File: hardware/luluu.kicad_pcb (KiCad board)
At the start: 2 copper layers, 75 x 30 mm, 53 parts, among them J1 BATT_CON, J2 RPi SWD, J3 STEMMA_{QT} I_{2}C, J4 Micro_SD_Card, J5 RPi UART, J6 USB_C_Receptacle_USB2.0, J7 DISP_LCD_ST7789, Q1 AO3401A, Q2 BSS138, SW1 SW_USBBOOT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

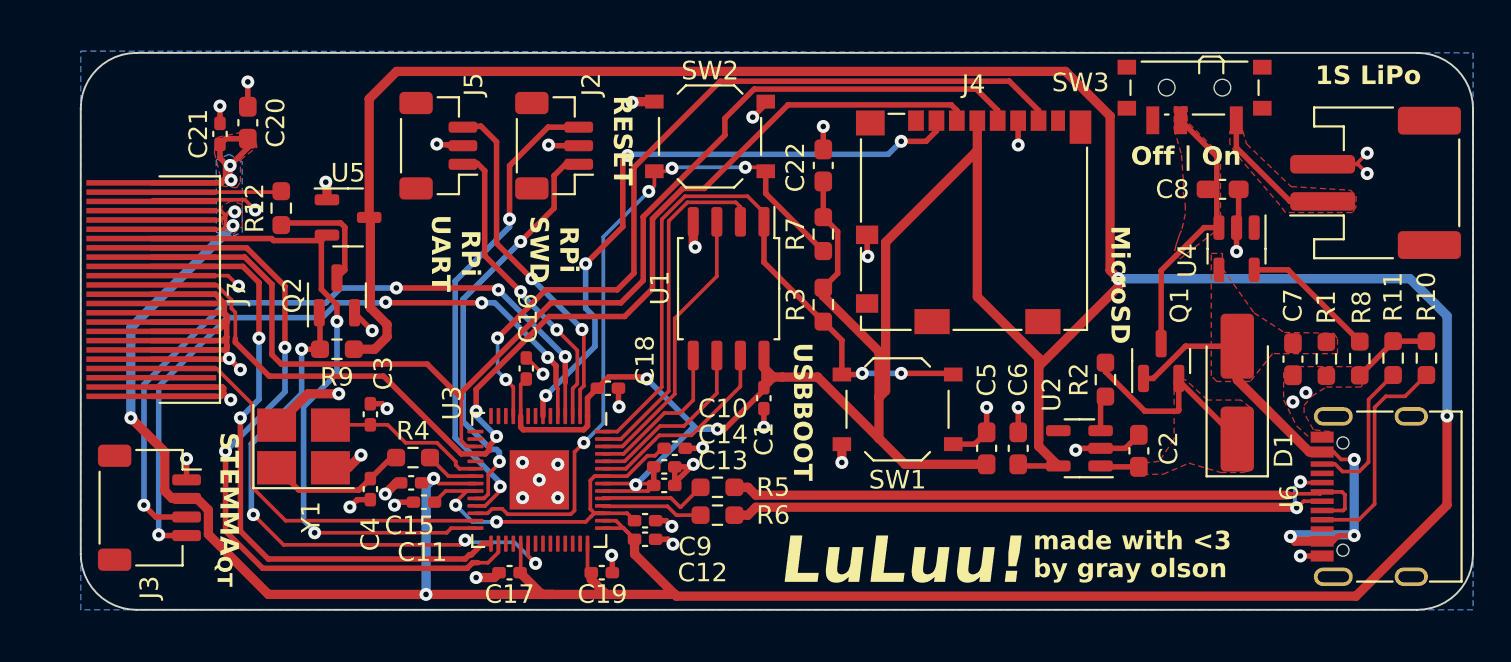
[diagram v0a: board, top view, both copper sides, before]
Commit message: layout improvements and jlcpcb part positioning offsets
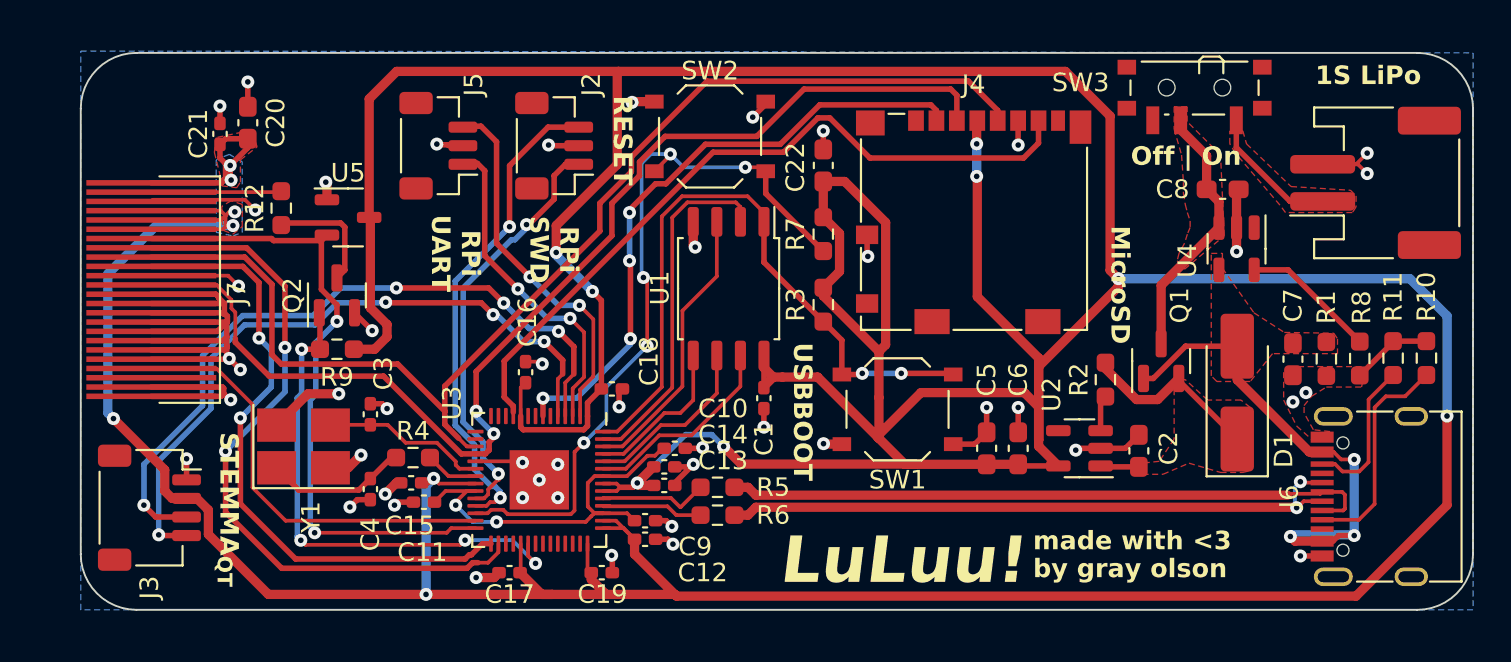
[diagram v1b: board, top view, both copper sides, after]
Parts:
- moved C18 0.22 mm to (140.8, 96.3)
- moved C16 0.20 mm to (136.2, 95.5)
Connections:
- U3 pad 19: unconnected-(U3-TESTEN-Pad19) -> GND
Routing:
- net +3V3: track 349.3 -> 380.0 mm, vias 12 -> 15
- net SPI_{MISO}: track 44.0 -> 39.6 mm, vias 2 -> 0
- net Net-(U3-RUN): track 37.5 -> 40.2 mm, vias 4 -> 5
- net DISP BACKLIGHT: track 30.7 -> 28.0 mm
- net GND: track 119.3 -> 121.6 mm
- net Net-(D1-K): track 13.7 -> 12.1 mm
- net UART_{TX}: track 19.0 -> 20.0 mm
- net UART_{RX}: track 16.7 -> 17.7 mm
- net SPI_{MOSI}: track 62.3 -> 63.2 mm
- net DISP ~{CS_{MAIN}}: track 38.9 -> 38.3 mm

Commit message: final_prod
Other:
- board text added: "+"
- board text added: "-"
- board text added: "v0"
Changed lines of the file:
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@@
     (effects (font (size 1 1) (thickness 0.2) bold) (justify left bottom))
   )
-  (gr_text "LuLuu!" (at 149.8375 107.05) (layer "F.SilkS")
+  (gr_text "+" (at 175.35 87.05) (layer "F.SilkS")
+    (effects (font (size 1.5 1.5) (thickness 0.3) bold) (justify left bottom))
+  )
+  (gr_text "LuLuu!" (at 148.45 107) (layer "F.SilkS")
     (effects (font (size 2.5 2.5) (thickness 0.4) bold italic) (justify left bottom))
   )
   (gr_text "RPi\nSWD" (at 136.3375 88.85 -90) (layer "F.SilkS")
     (effects (font (size 1 1) (thickness 0.2) bold) (justify bottom))
+  )
+  (gr_text "-" (at 177.2 85.35 90) (layer "F.SilkS")
+    (effects (font (size 1.5 1.5) (thickness 0.3) bold) (justify left bottom))
   )
   (gr_text "RESET" (at 140.8375 80.55 -90) (layer "F.SilkS")
@@
     (effects (font (size 1 1) (thickness 0.2) bold) (justify left bottom))
   )
+  (gr_text "v0" (at 160.65 106.85) (layer "F.SilkS")
+    (effects (font (size 1 1) (thickness 0.2) bold italic) (justify left bottom))
+  )
   (gr_text "RPi\nUART" (at 131.0375 89.05 -90) (layer "F.SilkS")

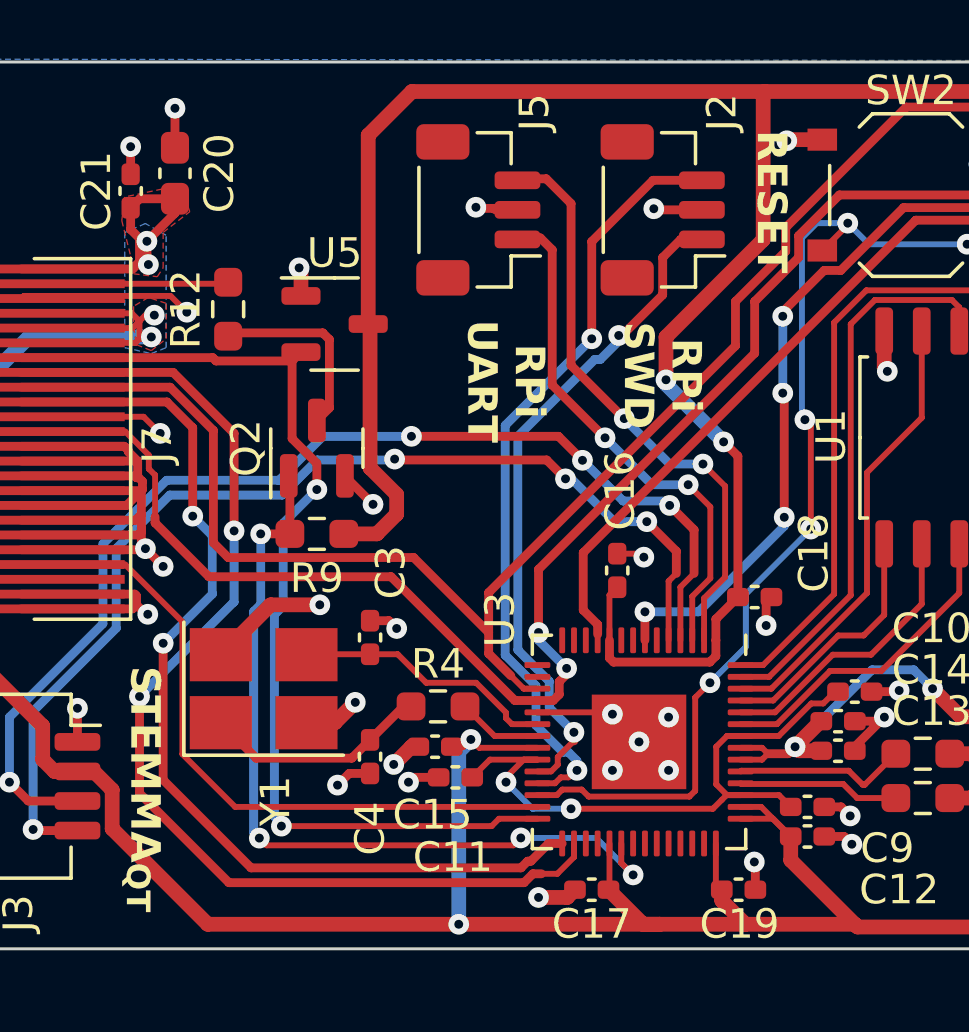
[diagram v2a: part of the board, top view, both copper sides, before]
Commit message: add pullups to disp reset, disp csmain, card cs
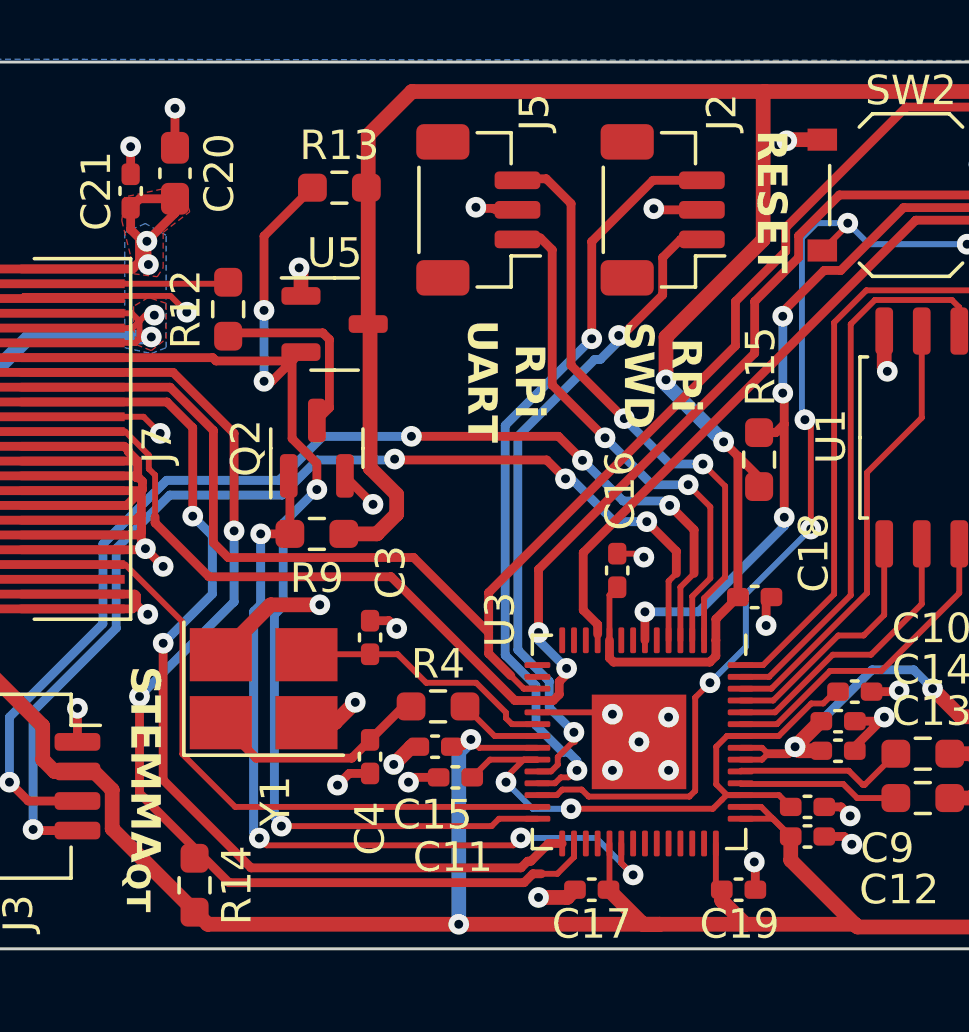
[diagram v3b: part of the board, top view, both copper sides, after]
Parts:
- added R13: 10k, Resistor_SMD:R_0603_1608Metric_Pad0.98x0.95mm_HandSolder, F.Cu at (126.8, 82.5)
- added R14: 10k, Resistor_SMD:R_0603_1608Metric_Pad0.98x0.95mm_HandSolder, F.Cu at (121.9, 106.1)
- added R15: 10k, Resistor_SMD:R_0603_1608Metric_Pad0.98x0.95mm_HandSolder, F.Cu at (141.0, 91.7)
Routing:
- net DISP ~{RESET}: track 35.1 -> 43.6 mm, vias 2 -> 4
- net +3V3: track 380.0 -> 381.3 mm
- net CARD ~{CS}: track 33.7 -> 34.7 mm

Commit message: rev1
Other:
- board text added: "v1"
- board text removed: "v0"
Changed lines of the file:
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@@
   (title_block
     (title "LuLuu!")
-    (date "2023-10-14")
-    (rev "0")
+    (date "2023-10-17")
+    (rev "1")
     (company "Gray Olson")
     (comment 1 "Made with love by")
@@
     (effects (font (size 1 1) (thickness 0.2) bold) (justify left bottom))
   )
-  (gr_text "v0" (at 160.65 106.85) (layer "F.SilkS")
+  (gr_text "v1" (at 160.65 106.85) (layer "F.SilkS")
     (effects (font (size 1 1) (thickness 0.2) bold italic) (justify left bottom))
   )

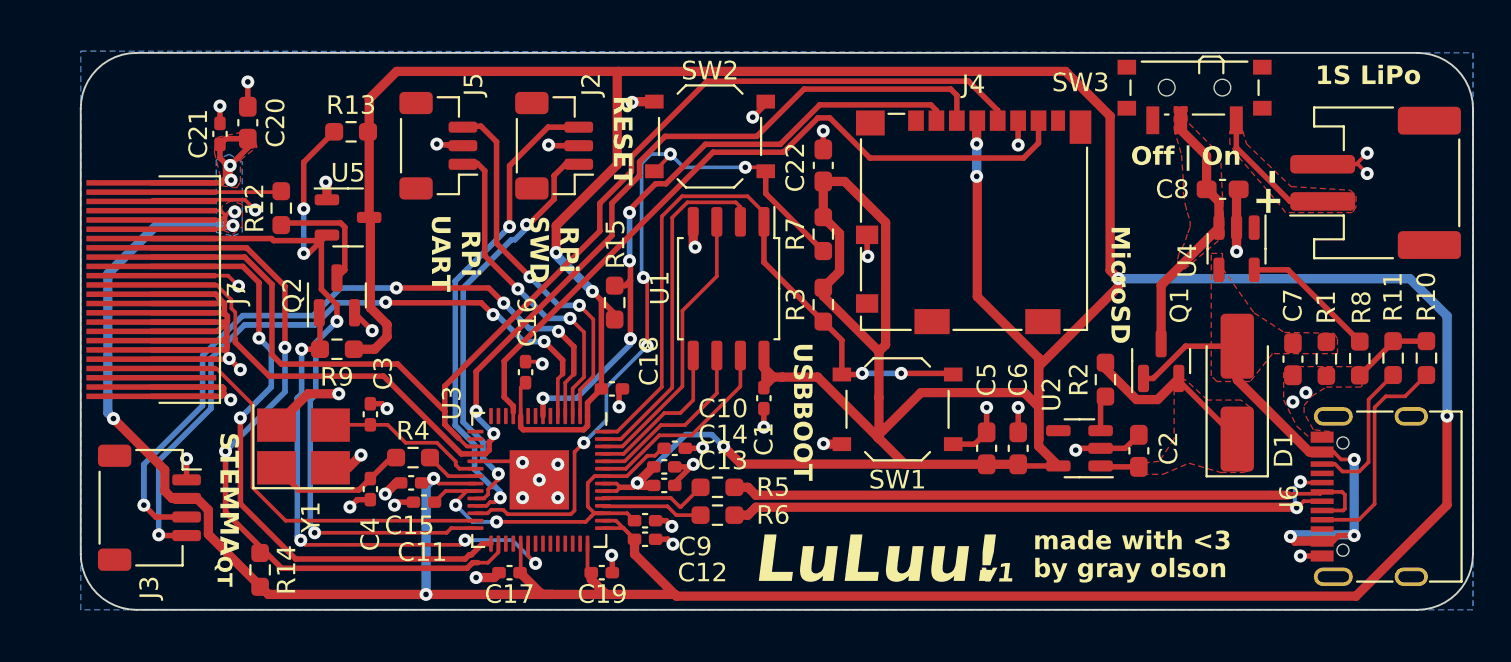
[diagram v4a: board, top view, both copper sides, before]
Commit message: rev1.1 - fix USB data and 1k boot resistor
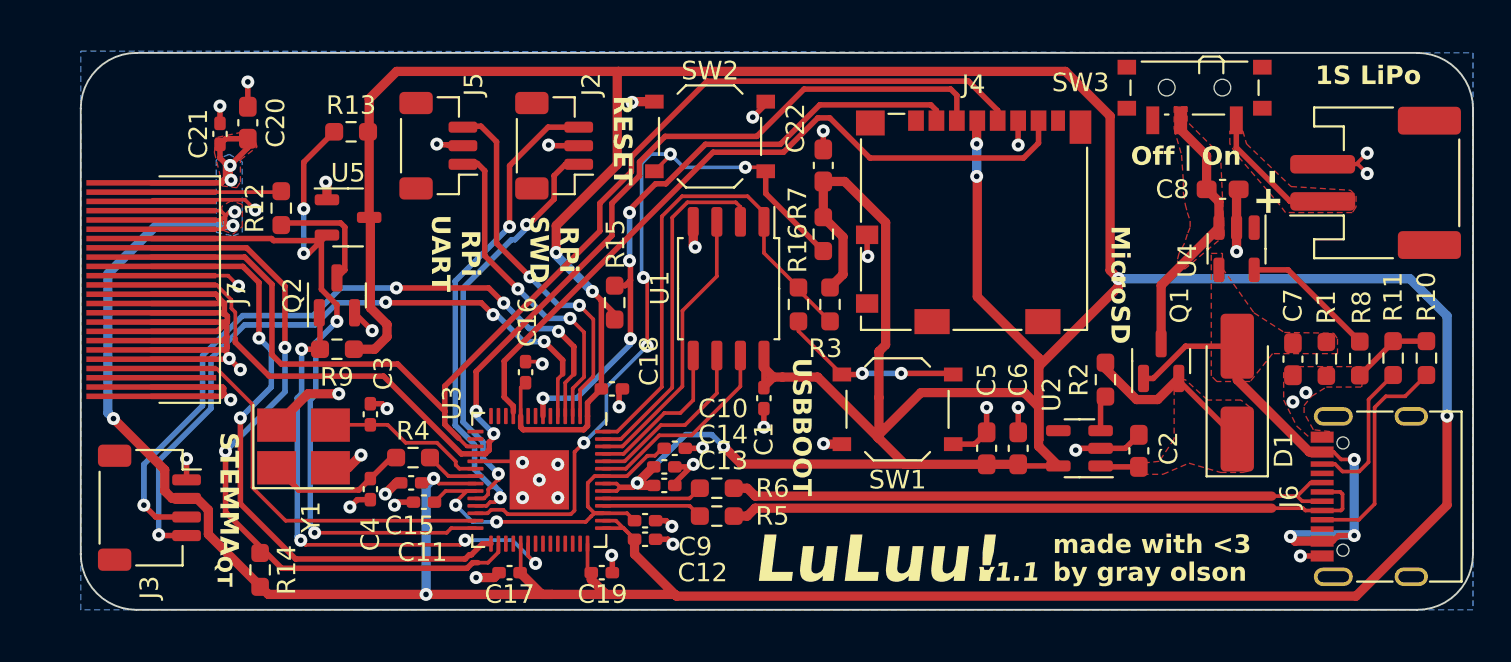
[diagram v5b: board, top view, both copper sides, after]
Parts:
- added R16: 1k, Resistor_SMD:R_0603_1608Metric_Pad0.98x0.95mm_HandSolder, F.Cu at (150.9, 91.8)
- moved R5 1.55 mm to (146.5, 103.2)
- moved R6 1.45 mm to (146.5, 101.7)
- moved R3 0.36 mm to (152.6, 91.8)
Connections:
- SW1 pad 1: Net-(U1-~{CS}) -> Net-(R16-Pad1)
- U3 pad 46: /USBR_D+ -> /USBR_D-
- U3 pad 47: /USBR_D- -> /USBR_D+
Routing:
- net Net-(R16-Pad1): track 0.00 -> 9.88 mm, vias 0 -> 2
- net Net-(U1-~{CS}): track 36.3 -> 27.2 mm, vias 2 -> 0
- net +3V3: track 381.3 -> 376.7 mm
- net USB_D+: track 34.7 -> 33.6 mm, vias 2 -> 0
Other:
- board text added: "v1.1"
- board text removed: "v1"

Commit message: start on rev2 of pcb
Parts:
- removed J5: RPi UART, Connector_JST:JST_SH_BM03B-SRSS-TB_1x03-1MP_P1.00mm_Vertical
- removed U5: APX803S-26/29, Package_TO_SOT_SMD:SOT-23-3
- moved R13 9.13 mm to (126.0, 91.6)
- moved Q2 4.58 mm to (126.0, 86.7)
- moved R9 4.46 mm to (126.0, 89.8)
- moved C16 0.29 mm to (135.9, 95.6)
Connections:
- net DISP BACKLIGHT renamed /DISP_BACKLIGHT
- net DISP CS_{DATA/~{CMD}} renamed /DISP_CS_{DATA/~{CMD}}
- net DISP VSYNC renamed /DISP_VSYNC
- net DISP ~{CS_{MAIN}} renamed /DISP_~{CS_{MAIN}}
- net DISP ~{RESET} renamed /DISP_~{RESET}
- net SWD renamed /SWD
- net SWD_{CLOCK} renamed /SWD_{CLOCK}
- net USB_D+ renamed /USB_D+
- net USB_D- renamed /USB_D-
- J3 pad 3: I_{2}C_{DATA} -> /I_{2}C_{DATA}
- J3 pad 4: I_{2}C_{CLOCK} -> /I_{2}C_{CLOCK}
- J4 pad 2: CARD ~{CS} -> /CARD_~{CS}
- J4 pad 3: SPI_{MOSI} -> /CARD_SPI_{MOSI}
- J4 pad 5: SPI_{CLOCK} -> /CARD_SPI_{CLOCK}
- J4 pad 7: SPI_{MISO} -> /CARD_SPI_{MISO}
- J7 pad 12: SPI_{MOSI} -> /DISP_SPI_{MOSI}
- J7 pad 9: SPI_{CLOCK} -> /DISP_SPI_{CLOCK}
- R15 pad 1: CARD ~{CS} -> /CARD_~{CS}
- U3 pad 11: SPI_{MISO} -> unconnected-(U3-GPIO8-Pad11)
- U3 pad 13: unconnected-(U3-GPIO10-Pad13) -> /I_{2}C_{DATA}
- U3 pad 14: unconnected-(U3-GPIO11-Pad14) -> /I_{2}C_{CLOCK}
- U3 pad 17: SPI_{CLOCK} -> /DISP_SPI_{CLOCK}
- U3 pad 18: SPI_{MOSI} -> /DISP_SPI_{MOSI}
- U3 pad 2: UART_{TX} -> unconnected-(U3-GPIO0-Pad2)
- U3 pad 3: UART_{RX} -> /CARD_~{CS}
- U3 pad 4: I_{2}C_{DATA} -> /CARD_SPI_{CLOCK}
- U3 pad 5: I_{2}C_{CLOCK} -> /CARD_SPI_{MOSI}
- U3 pad 6: unconnected-(U3-GPIO4-Pad6) -> /CARD_SPI_{MISO}
- U3 pad 7: CARD ~{CS} -> unconnected-(U3-GPIO5-Pad7)
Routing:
- net +3V3: track 376.7 -> 176.8 mm, vias 15 -> 11
- net SPI_{CLOCK}: track 64.8 -> 0.00 mm
- net SPI_{MOSI}: track 63.2 -> 0.00 mm, vias 2 -> 0
- net /CARD_SPI_{MISO}: track 0.00 -> 40.7 mm
- net SPI_{MISO}: track 39.6 -> 0.00 mm
- net I_{2}C_{DATA}: track 38.7 -> 0.00 mm, vias 4 -> 0
- net I_{2}C_{CLOCK}: track 36.8 -> 0.00 mm, vias 4 -> 0
- net /CARD_SPI_{CLOCK}: track 0.00 -> 36.1 mm
- net CARD ~{CS}: track 34.7 -> 0.00 mm, vias 4 -> 0
- net /CARD_SPI_{MOSI}: track 0.00 -> 34.6 mm
- net /CARD_~{CS}: track 0.00 -> 32.4 mm, vias 0 -> 2
- net /DISP_SPI_{CLOCK}: track 0.00 -> 24.2 mm
- net /DISP_SPI_{MOSI}: track 0.00 -> 22.6 mm
- net UART_{TX}: track 20.0 -> 0.00 mm, vias 2 -> 0
- net UART_{RX}: track 17.7 -> 0.00 mm, vias 2 -> 0
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- added copper zone on In1.Cu, net GND
- added copper zone on In2.Cu, net GND
- removed copper zone on B.Cu, net GND
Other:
- copper layers 2 -> 4
- board text removed: "RPi UART"

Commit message: pcb rev 2.0 progress
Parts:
- added D2: CHRG, LED_SMD:LED_0805_2012Metric_Pad1.15x1.40mm_HandSolder, F.Cu at (171.0, 94.5)
- added R17: 1k, Resistor_SMD:R_0603_1608Metric_Pad0.98x0.95mm_HandSolder, F.Cu at (169.0, 94.8)
- moved J4 27.3 mm to (133.1, 88.2)
- moved C22 27.0 mm to (125.3, 82.2), turned to -90 degrees
- moved R8 23.3 mm to (157.9, 92.1)
- moved C7 20.9 mm to (158.7, 85.6), turned to 0 degrees
- moved R15 19.8 mm to (123.5, 82.2), turned to 90 degrees
- moved R10 17.7 mm to (167.1, 94.8)
- moved R11 17.5 mm to (165.4, 94.8)
- moved R1 17.2 mm to (162.2, 96.9), turned to 180 degrees
- moved SW3 15.6 mm to (156.6, 80.4)
- moved C2 15.4 mm to (154.9, 93.8), turned to 0 degrees
- moved U4 15.4 mm to (159.1, 88.4), turned to 180 degrees
- moved D1 15.3 mm to (159.6, 99.7), turned to 0 degrees
- moved C5 15.0 mm to (154.9, 85.9), turned to 0 degrees
- moved SW1 15.0 mm to (149.2, 84.2), turned to 90 degrees
- moved C6 14.3 mm to (154.9, 87.6), turned to 0 degrees
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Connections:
- C5 pad 1: +3V3 -> Net-(SW3-A)
- C6 pad 1: +3V3 -> Net-(SW3-A)
- J1 pad 1: Net-(J1-Pin_1) -> +BATT
- SW3 pad 1: Net-(J1-Pin_1) -> Net-(SW3-A)
- SW3 pad 2: +BATT -> +3V3
- U2 pad 5: +3V3 -> Net-(SW3-A)
- U3 pad 2: unconnected-(U3-GPIO0-Pad2) -> /CARD_SPI_{MISO}
- U3 pad 3: /CARD_~{CS} -> unconnected-(U3-GPIO1-Pad3)
- U3 pad 6: /CARD_SPI_{MISO} -> unconnected-(U3-GPIO4-Pad6)
- U3 pad 7: unconnected-(U3-GPIO5-Pad7) -> /CARD_~{CS}
- U4 pad 1: unconnected-(U4-~{CHRG}-Pad1) -> Net-(D2-K)
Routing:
- net +3V3: track 176.8 -> 266.1 mm, vias 11 -> 8
- net /CARD_SPI_{MISO}: track 40.7 -> 16.2 mm
- net /I_{2}C_{DATA}: track 1.56 -> 25.5 mm, vias 1 -> 2
- net /I_{2}C_{CLOCK}: track 0.00 -> 23.5 mm, vias 0 -> 2
- net /CARD_SPI_{CLOCK}: track 36.1 -> 15.7 mm
- net +5V: track 26.9 -> 45.0 mm, vias 3 -> 5
- net /CARD_SPI_{MOSI}: track 34.6 -> 16.5 mm
- net Net-(D2-K): track 0.00 -> 12.5 mm, vias 0 -> 2
- net GND: track 117.5 -> 106.0 mm
- net /USB_D+: track 35.0 -> 23.7 mm
- net /USB_D-: track 34.6 -> 23.7 mm
- net Net-(SW3-A): track 0.00 -> 10.4 mm
- net Net-(R16-Pad1): track 9.88 -> 20.1 mm
- net Net-(J1-Pin_1): track 7.32 -> 0.00 mm
- net /CARD_~{CS}: track 32.4 -> 25.3 mm, vias 2 -> 0
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- removed copper zone on F.Cu, net +5V
- removed copper zone on F.Cu, net +BATT
- removed copper zone on F.Cu, net GND
- removed copper zone on F.Cu, net Net-(D1-K)
- removed copper zone on F.Cu, net Net-(J1-Pin_1)
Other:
- board size 75 x 30 mm -> 64.1 x 30 mm
- board text added: "BOOT"
- board text added: "CHRG"
- board text added: "v2.0"
- board text added: "µSD"
- board text removed: "MicroSD"
- board text removed: "USBBOOT"
- board text removed: "v1.1"
